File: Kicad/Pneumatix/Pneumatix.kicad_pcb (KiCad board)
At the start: 2 copper layers, 33 x 57.1 mm, 16 parts, among them J1 436500404, J2 142-0701-801, J3 Conn_01x04_Socket, U1 E22-400T33S

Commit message: wip: pcb components
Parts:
- JP1, JP2: moved to B.Cu
- moved JP1 26.2 mm to (22.1, 29.0), turned to 180 degrees
- moved JP2 23.2 mm to (22.1, 31.6), turned to 180 degrees
- moved D1 5.71 mm to (2.67, 50.7)
- moved C1 5.24 mm to (6.22, 50.7)
- moved R3 5.04 mm to (4.57, 50.7), turned to -90 degrees
- moved R2 4.05 mm to (30.3, 41.1), turned to 0 degrees
- moved R4 2.68 mm to (30.3, 42.8), turned to 0 degrees
- moved C2 2.43 mm to (7.87, 50.7), turned to 90 degrees
- moved H2 2.41 mm to (3.81, 55.8)
- moved J1 2.22 mm to (22.4, 50.3)
- moved D2 1.44 mm to (30.4, 44.5), turned to 0 degrees
- moved U1 1.14 mm to (26.9, 48.6)
- moved J2 0.70 mm to (23.1, 3.05)
- moved J3 0.57 mm to (30.1, 17.1)
- moved H3 0.46 mm to (30.1, 23.9)
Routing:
- net +5V: track 0.00 -> 3.32 mm
- net Net-(D1-A): track 0.00 -> 2.57 mm
- net GND: track 0.00 -> 1.65 mm
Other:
- board size 33 x 57.1 mm -> 33.1 x 59.4 mm

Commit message: wip: pcb traces and plane
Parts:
- moved JP1 6.35 mm to (15.7, 29.0)
- moved JP2 6.35 mm to (15.7, 31.6)
- moved R2 1.93 mm to (30.6, 39.2)
- moved R4 1.93 mm to (30.6, 40.9)
- moved C1 1.66 mm to (7.87, 50.5), turned to -90 degrees
- moved C2 1.66 mm to (6.22, 50.5), turned to -90 degrees
- moved D2 0.92 mm to (30.6, 43.6), turned to 90 degrees
- moved D1 0.13 mm to (2.67, 50.5), turned to 90 degrees
- moved R3 0.13 mm to (4.57, 50.5), turned to 90 degrees
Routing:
- net +5V: track 3.32 -> 77.0 mm
- net LORA_RX: track 0.00 -> 51.2 mm, vias 0 -> 3
- net LORA_TX: track 0.00 -> 44.6 mm, vias 0 -> 3
- net GND: track 1.65 -> 14.5 mm, vias 0 -> 39
- net Net-(JP1-A): track 0.00 -> 10.6 mm, vias 0 -> 1
- net Net-(JP2-A): track 0.00 -> 10.6 mm, vias 0 -> 1
- net Net-(U1-ANT): track 0.00 -> 5.86 mm
- net Net-(U1-AUX): track 0.00 -> 4.53 mm
- net Net-(D2-A): track 0.00 -> 3.87 mm
- added copper zone on B.Cu, net GND
- added copper zone on F.Cu, net GND
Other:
- outline, holes or cut-outs redrawn

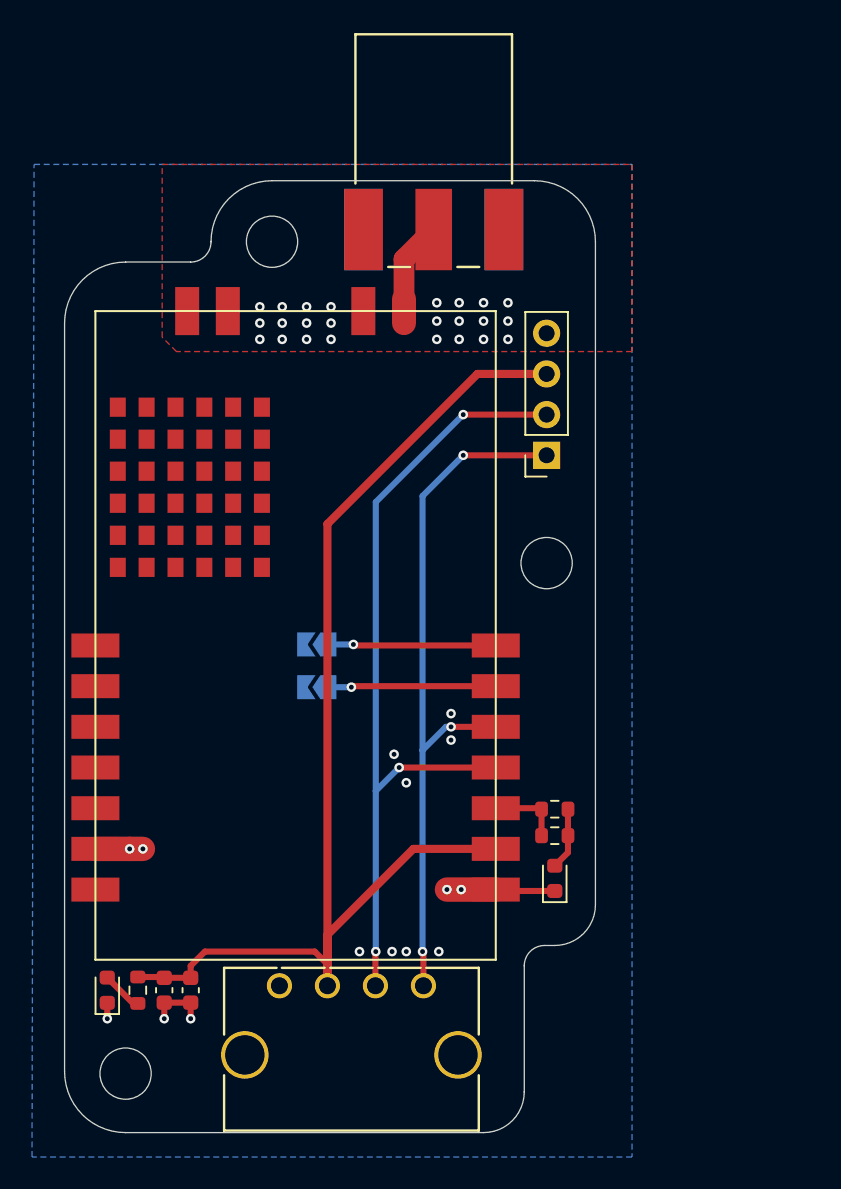
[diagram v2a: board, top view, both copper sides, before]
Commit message: wip: ajust e22 position and add silkscreen
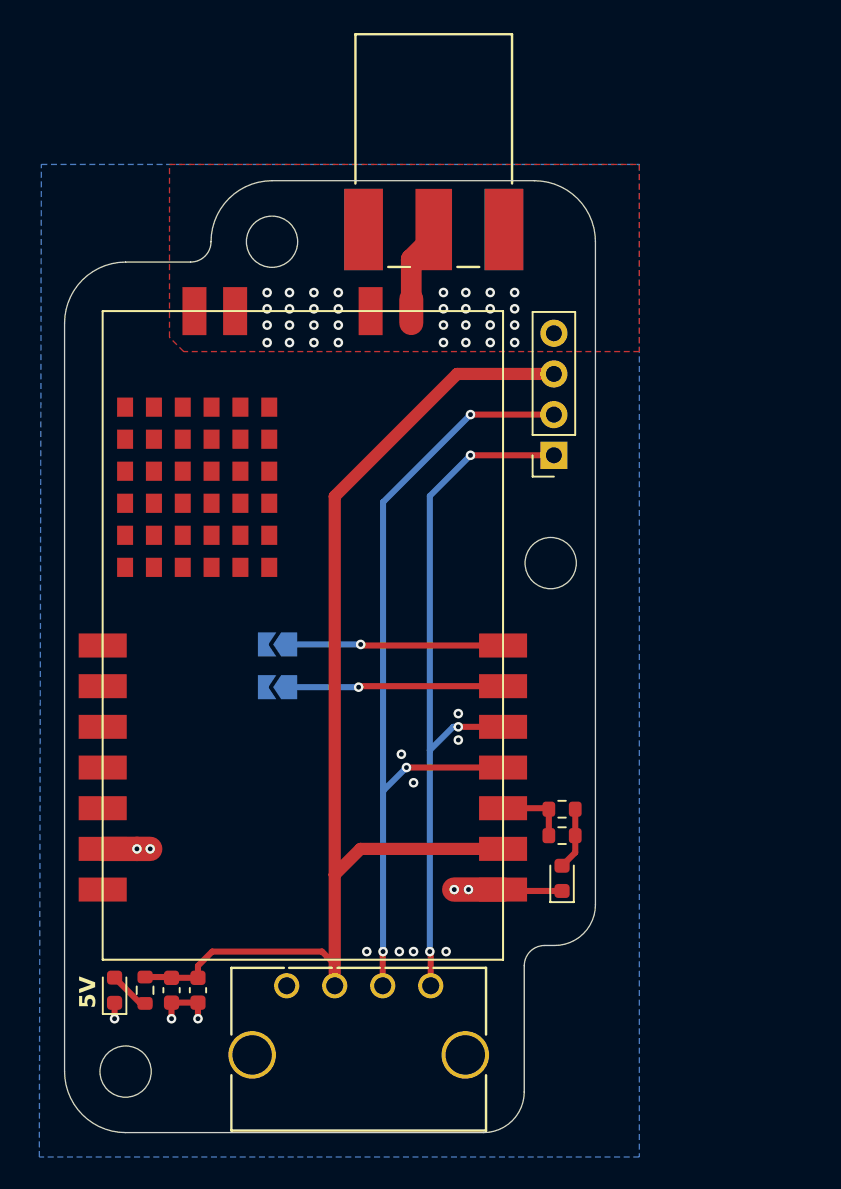
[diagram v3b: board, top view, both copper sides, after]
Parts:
- moved JP1 2.45 mm to (13.3, 29.0)
- moved JP2 2.45 mm to (13.3, 31.6)
- moved D2 0.46 mm to (31.1, 43.6)
- moved R2 0.46 mm to (31.1, 39.2)
- moved R4 0.46 mm to (31.1, 40.9)
- moved U1 0.46 mm to (27.4, 48.6)
- moved C1 0.46 mm to (8.33, 50.5)
- moved C2 0.46 mm to (6.68, 50.5)
- moved D1 0.46 mm to (3.12, 50.5)
- moved R3 0.46 mm to (5.03, 50.5)
- moved J1 0.46 mm to (22.9, 50.3)
- moved J3 0.46 mm to (30.6, 17.1)
- moved H3 0.25 mm to (30.4, 23.9)
- moved H2 0.13 mm to (3.81, 55.6)
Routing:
- net +5V: track 77.0 -> 73.2 mm
- net Net-(JP1-A): track 10.6 -> 13.5 mm
- net Net-(JP2-A): track 10.6 -> 13.5 mm
- net GND: vias 39 -> 47
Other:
- board text added: "5V"
- board text added: "5V+"
- board text added: "GND"
- board text added: "M0"
- board text added: "M1"
- board text added: "RX"
- board text added: "TX"

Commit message: wip: add thermal pads and plane for heat dissipation
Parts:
- moved C1 0.41 mm to (8.74, 50.5)
- moved C2 0.41 mm to (7.09, 50.5)
- moved R3 0.30 mm to (4.72, 50.5)
- moved D1 0.07 mm to (3.05, 50.5)
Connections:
- U1 pad 0: (no net) -> GND
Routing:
- net GND: track 14.5 -> 11.5 mm, vias 47 -> 137
- net +5V: track 73.2 -> 74.7 mm
- net LORA_RX: track 51.2 -> 51.8 mm
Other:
- board text added: "AUX"

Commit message: wip: add pu/pd for M0 and M1, remake traces and swap gnd/signal/passive components plane
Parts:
- added R5: 1.5k, Resistor_SMD:R_0603_1608Metric, B.Cu at (20.5, 31.6)
- added R6: 1.5k, Resistor_SMD:R_0603_1608Metric, B.Cu at (20.5, 33.3)
- added R7: 1.5k, Resistor_SMD:R_0603_1608Metric, B.Cu at (20.5, 29.0)
- added R8: 1.5k, Resistor_SMD:R_0603_1608Metric, B.Cu at (20.5, 27.3)
- J3: value Conn_01x04_Socket -> Conn_01x06_Socket; footprint Connector_PinSocket_2.54mm:PinSocket_1x04_P2.54mm_Vertical -> Connector_PinHeader_2.54mm:PinHeader_1x06_P2.54mm_Vertical
- R2, R4: moved to B.Cu
- moved R2 6.82 mm to (24.2, 39.2), turned to 180 degrees
- moved R4 6.82 mm to (24.2, 40.8), turned to 180 degrees
- moved JP1 4.71 mm to (17.2, 31.6)
- moved JP2 4.69 mm to (17.2, 29.0)
- moved D2 4.45 mm to (28.5, 47.2)
- moved J3 4.12 mm to (30.1, 21.2)
- moved H3 1.50 mm to (30.1, 25.3)
- moved J2 1.41 mm to (21.6, 3.10)
- moved H1 1.32 mm to (11.6, 3.81)
- turned D1 to -90 degrees
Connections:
- J3 pad 1: LORA_TX -> LORA_M1
- J3 pad 2: LORA_RX -> LORA_M0
- J3 pad 3: +5V -> LORA_TX
- J3 pad 4: GND -> LORA_RX
- JP1 pad 2: GND -> +5V
- JP2 pad 2: GND -> +5V
- U1 pad 6: Net-(JP2-A) -> LORA_M1
- U1 pad 7: Net-(JP1-A) -> LORA_M0
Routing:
- net LORA_M0: track 0.00 -> 23.0 mm, vias 0 -> 1
- net LORA_M1: track 0.00 -> 22.5 mm, vias 0 -> 1
- net LORA_TX: track 45.1 -> 61.4 mm, vias 3 -> 1
- net Net-(JP2-A): track 13.5 -> 1.83 mm, vias 1 -> 0
- net Net-(JP1-A): track 13.5 -> 1.83 mm, vias 1 -> 0
- net LORA_RX: track 51.8 -> 61.8 mm, vias 3 -> 1
- net GND: track 11.5 -> 1.80 mm, vias 137 -> 39
- net Net-(D2-A): track 3.87 -> 10.5 mm, vias 0 -> 1
- net +5V: track 74.7 -> 79.1 mm, vias 0 -> 1
- net Net-(U1-ANT): track 5.86 -> 5.03 mm
- net Net-(U1-AUX): track 4.53 -> 5.35 mm, vias 0 -> 1
- net Net-(D1-A): track 2.34 -> 1.64 mm
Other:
- board size 33.1 x 59.4 mm -> 33.9 x 59.4 mm

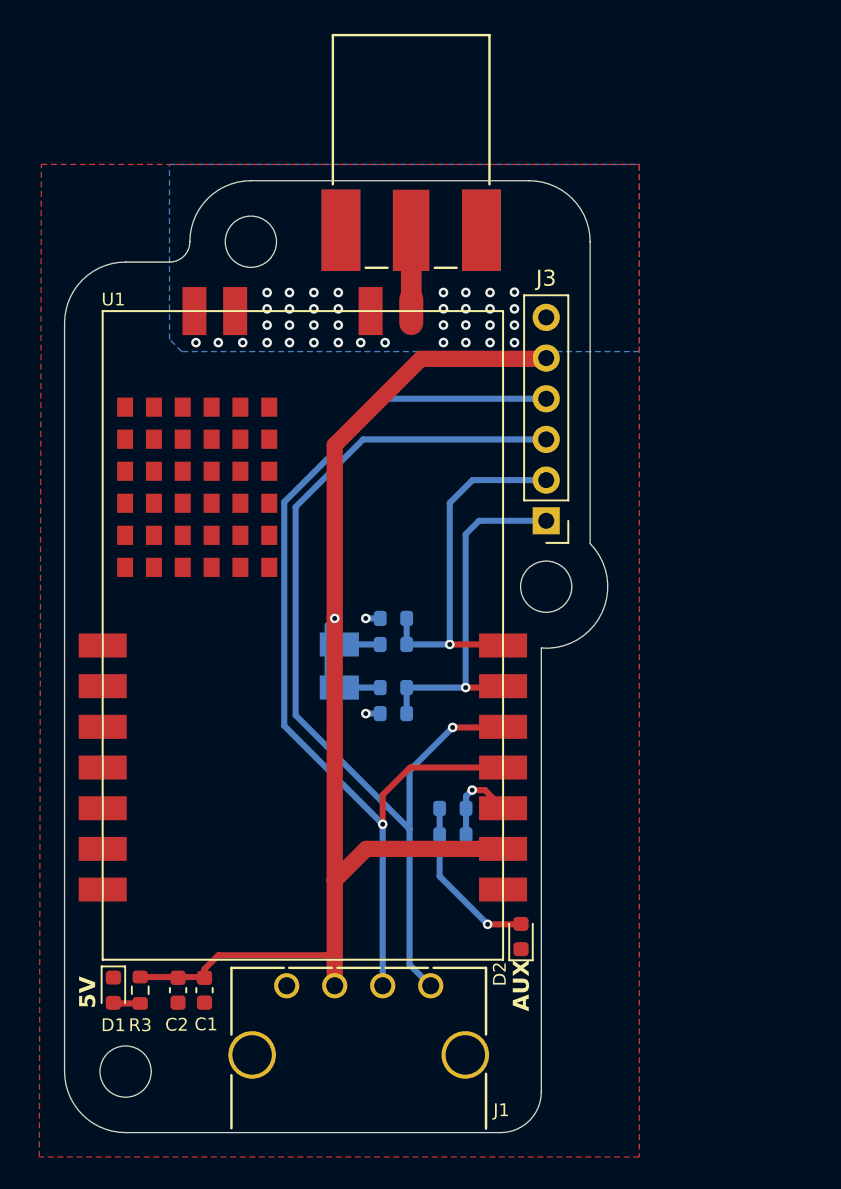
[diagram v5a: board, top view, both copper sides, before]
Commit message: wip: fix voltage divider for m0 and m1, reduce 2.54 debug header to 2.00mm
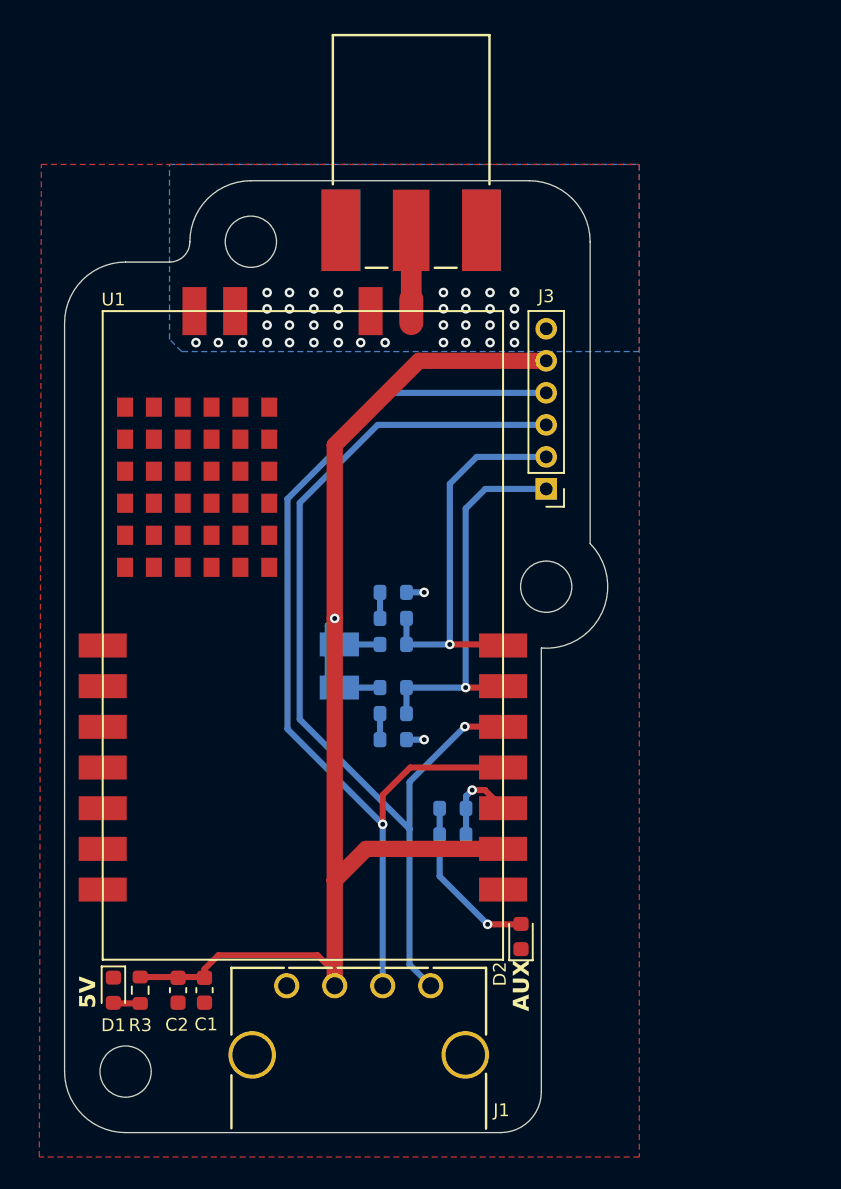
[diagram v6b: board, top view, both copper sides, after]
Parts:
- added R10: 1.5k, Resistor_SMD:R_0603_1608Metric, B.Cu at (20.5, 25.7)
- added R9: 1.5k, Resistor_SMD:R_0603_1608Metric, B.Cu at (20.5, 34.9)
- J3: footprint Connector_PinHeader_2.54mm:PinHeader_1x06_P2.54mm_Vertical -> Connector_PinHeader_2.00mm:PinHeader_1x06_P2.00mm_Vertical
- moved J3 1.99 mm to (30.1, 19.2)
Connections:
- R6 pad 2: GND -> Net-(R6-Pad2)
- R8 pad 2: GND -> Net-(R10-Pad1)
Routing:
- net LORA_M1: track 22.5 -> 24.3 mm
- net Net-(R10-Pad1): track 0.00 -> 1.63 mm
- net Net-(R6-Pad2): track 0.00 -> 1.63 mm
- net LORA_M0: track 23.0 -> 24.3 mm

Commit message: FIX: fixed 5V trace cutting ground plane and minor routing rework
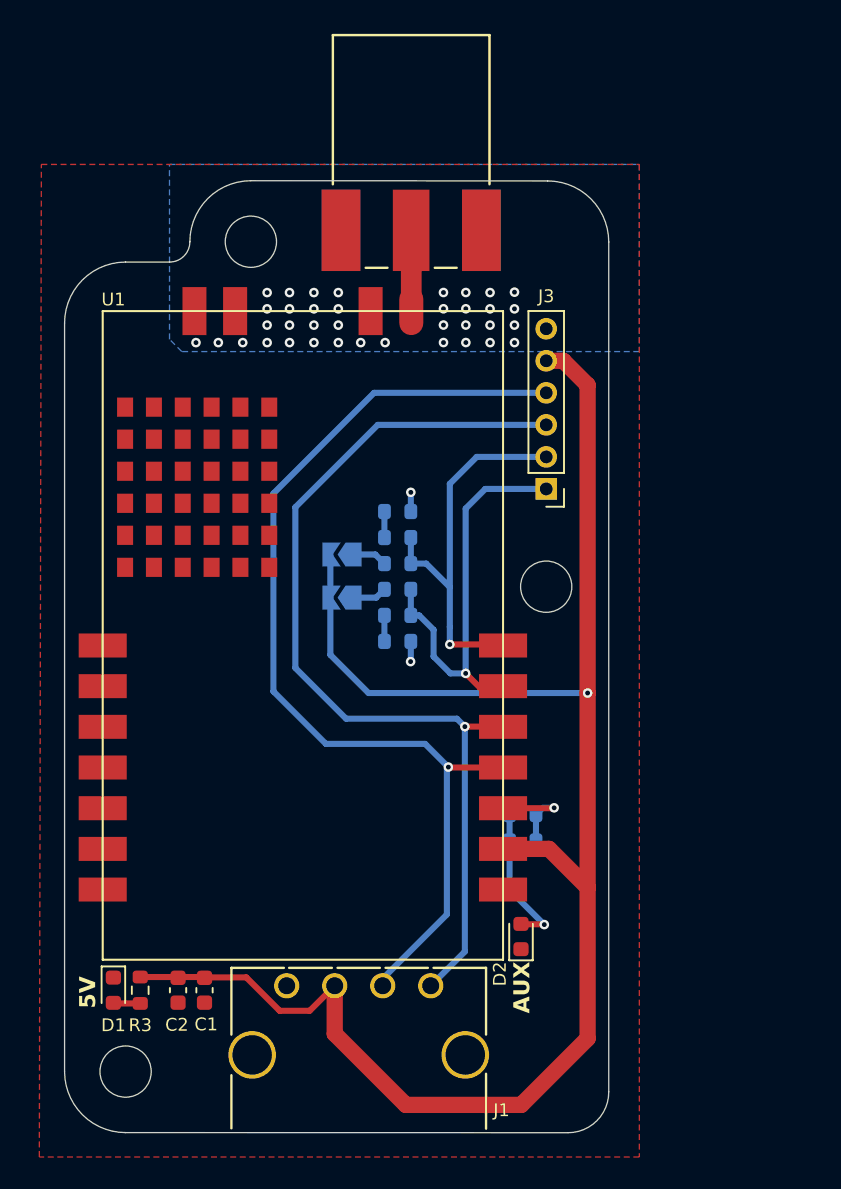
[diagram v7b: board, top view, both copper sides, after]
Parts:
- moved R5 6.14 mm to (20.8, 25.5)
- moved R6 6.14 mm to (20.8, 27.1)
- moved R9 6.14 mm to (20.8, 28.8)
- moved JP2 5.62 mm to (17.3, 23.3)
- moved JP1 5.62 mm to (17.3, 26.0)
- moved R8 5.06 mm to (20.8, 22.3)
- moved R10 5.06 mm to (20.8, 20.7)
- moved R7 5.06 mm to (20.8, 23.9)
- moved R2 4.38 mm to (28.6, 39.6)
- moved R4 4.38 mm to (28.6, 41.2)
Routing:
- net +5V: track 79.2 -> 109.6 mm
- net LORA_RX: track 61.8 -> 63.7 mm
- net LORA_TX: track 61.2 -> 59.4 mm
- net LORA_M1: track 24.3 -> 26.0 mm
- net Net-(D2-A): track 10.5 -> 9.26 mm
- net Net-(U1-AUX): track 5.35 -> 6.16 mm
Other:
- board size 33.9 x 59.4 mm -> 34 x 59.4 mm

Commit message: wip: silkscreen and adjustements
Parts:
- added G***: LOGO, Pneumatix_Lib:Logo-QC, B.Cu at (5.39, 19.0)
- added G***: LOGO, Pneumatix_Lib:Logo-Pneumatix, B.Cu at (18.9, 22.4)
- added G***: LOGO, Pneumatix_Lib:Logo-GAUL, B.Cu at (3.20, 42.6)
- moved D2 0.30 mm to (3.35, 50.5)
- moved R9 0.28 mm to (5.00, 50.5)
- moved C1 0.24 mm to (8.50, 50.5)
- moved C2 0.24 mm to (6.85, 50.5)
- renumbered D2 to D1, D1 to D2, H3 to H2, H2 to H3, J3 to J1, J1 to J2, J2 to J3, R4 to R1, R5 to R3, R7 to R4, R6 to R5, R9 to R6, R8 to R7, R10 to R8, R3 to R9
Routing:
- net GND: track 2.44 -> 5.70 mm, vias 39 -> 40
- net Net-(D1-A): track 9.26 -> 7.12 mm
- net Net-(U1-AUX): track 6.16 -> 5.52 mm
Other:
- outline, holes or cut-outs redrawn
- board text added: "ID"
- board text added: "Pneuamtix"
- board text added: "Samuel Gagnon Victor Deschênes 09-2026 V1"
